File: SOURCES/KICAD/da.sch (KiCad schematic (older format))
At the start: 152 parts, among them IC301 IC_OPA1652AIDR, IC302 IC_OPA1652AIDR, IC303 IC_OPA1652AIDR, IC304 IC_OPA1652AIDR, IC305 IC_AK4458VN, IC306 IC_OPA1652AIDR, IC307 IC_OPA1652AIDR, IC308 IC_OPA1652AIDR, IC309 IC_OPA1652AIDR, X301 CONN_02X13

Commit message: Updated BOM
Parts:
- C301, C302, C309, C310, C314, C315, C321, C324, C325, C329, C330, C331, C340, C341, C345, C346, C347, C353, C356, C357: Manufacturer (none) -> Nichicon; digikey 399-6102-ND -> UVY1E101MDD-ND; pn (none) -> UVY1E101MDD
- C303, C304, C311, C312, C316, C317, C326, C327, C332, C333, C342, C343, C348, C349, C358, C359: Manufacturer (none) -> Panasonic Electronic Components; pn (none) -> ECH-U1H471GX5
- C305, C306, C318, C319, C334, C335, C350, C351: Manufacturer (none) -> KEMET; pn (none) -> C0805C270J5GACTU
- C307, C308, C322, C323, C338, C339, C354, C355: Manufacturer (none) -> Panasonic Electronic Components; pn (none) -> ECH-U1C392JX5
- C313: Manufacturer (none) -> Yageo; pn (none) -> CC0805KKX7R7BB105
- C320, C328, C336, C344, C352, C361, C362, C363, C364, C365, C366, C367, C368, C369: Manufacturer (none) -> KEMET; pn (none) -> C0805C104K5RACTU
- C337, C360: Manufacturer (none) -> Murata Electronics North America; pn (none) -> GRM21BR61E106MA73L
- IC301, IC302, IC303, IC304, IC306, IC307, IC308, IC309: Manufacturer (none) -> Texas Instruments; pn (none) -> OPA1652AIDR
- IC305: Manufacturer (none) -> AKM Semiconductor Inc.; pn (none) -> AK4458VN
- R301, R303, R311, R313, R317, R319, R328, R330, R335, R337, R345, R347, R352, R354, R368, R370: Manufacturer (none) -> Susumu; pn (none) -> RR1220P-4421-D-M
- R302, R304, R315, R316, R318, R320, R332, R333, R336, R338, R350, R351, R353, R355, R372, R373: Manufacturer (none) -> Susumu; pn (none) -> RR1220P-3401-D-M
- R305, R306, R312, R314, R321, R322, R329, R331, R339, R340, R346, R348, R357, R358, R369, R371: Manufacturer (none) -> Stackpole Electronics Inc.; pn (none) -> RNCP0805FTD150R
- R307, R308, R309, R310, R324, R325, R326, R327, R341, R342, R343, R344, R364, R365, R366, R367: Manufacturer (none) -> Yageo; pn (none) -> RT0805FRE074K7L
- R323, R334, R349, R356: Manufacturer (none) -> Yageo; pn (none) -> RC0805FR-0720RL
- R359, R360, R361, R362, R363: Manufacturer (none) -> Yageo; pn (none) -> RC0805JR-070RL
- X301: Manufacturer (none) -> Sullins Connector Solutions; pn (none) -> PRPC013DAAN-RC

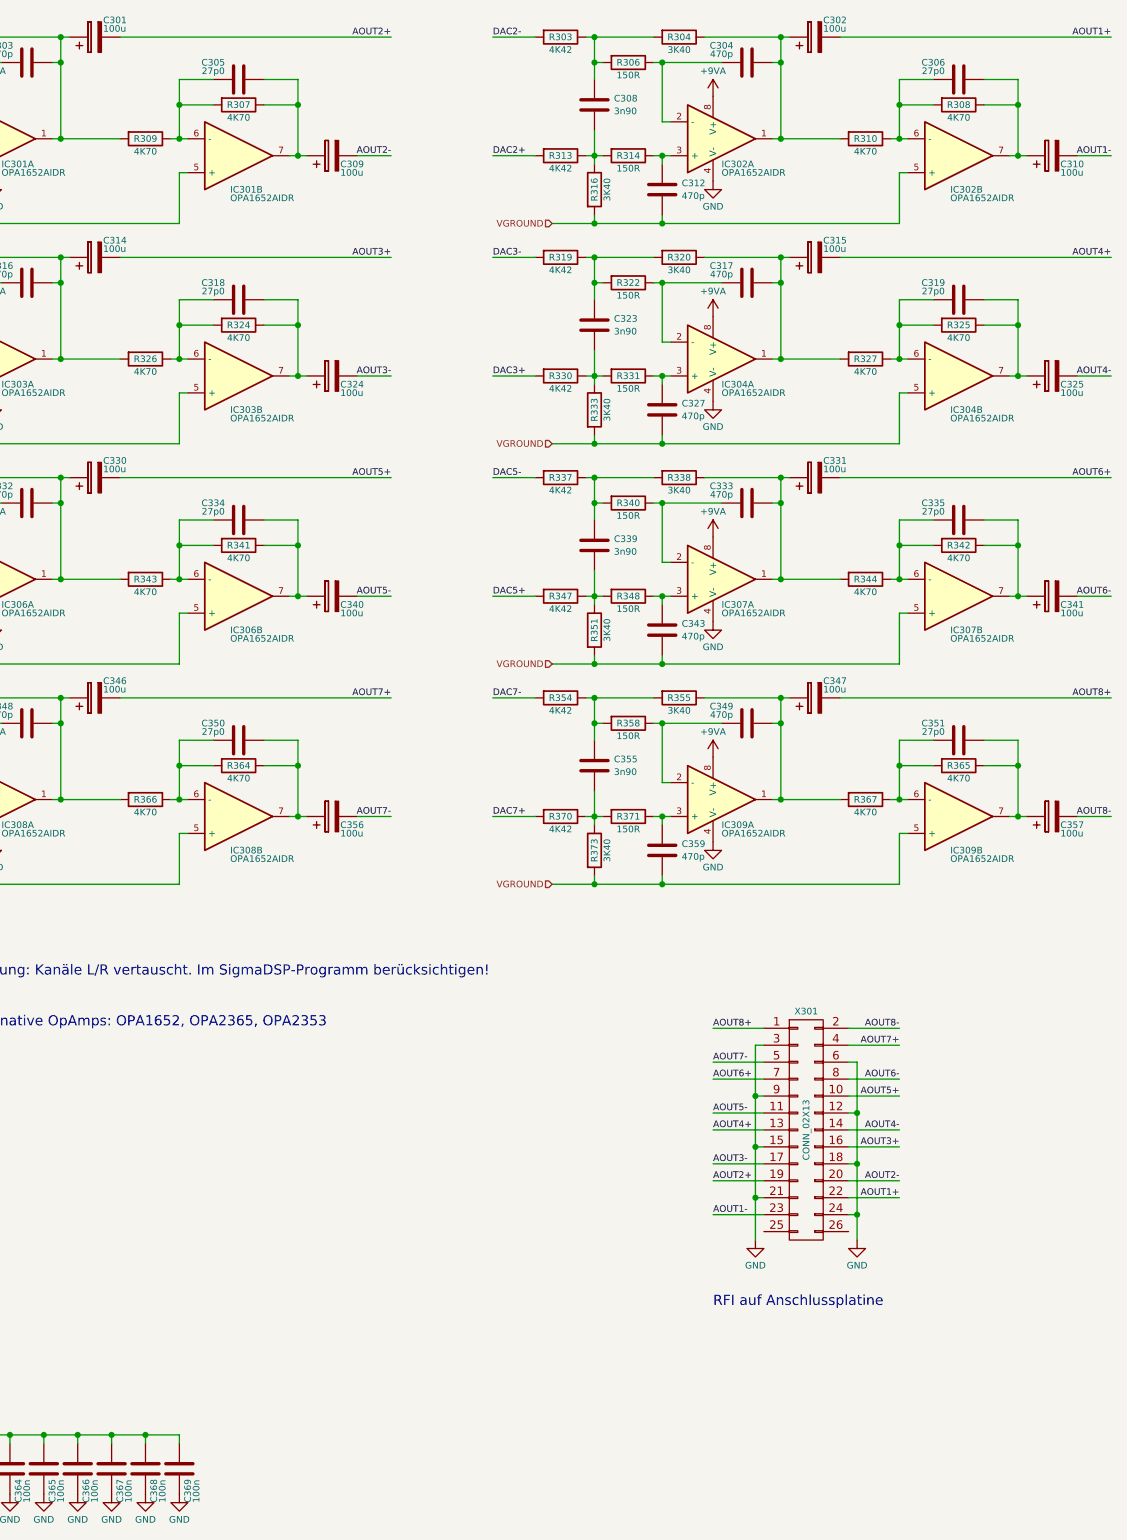
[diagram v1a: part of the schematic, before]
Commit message: Optimized DAC Output filter
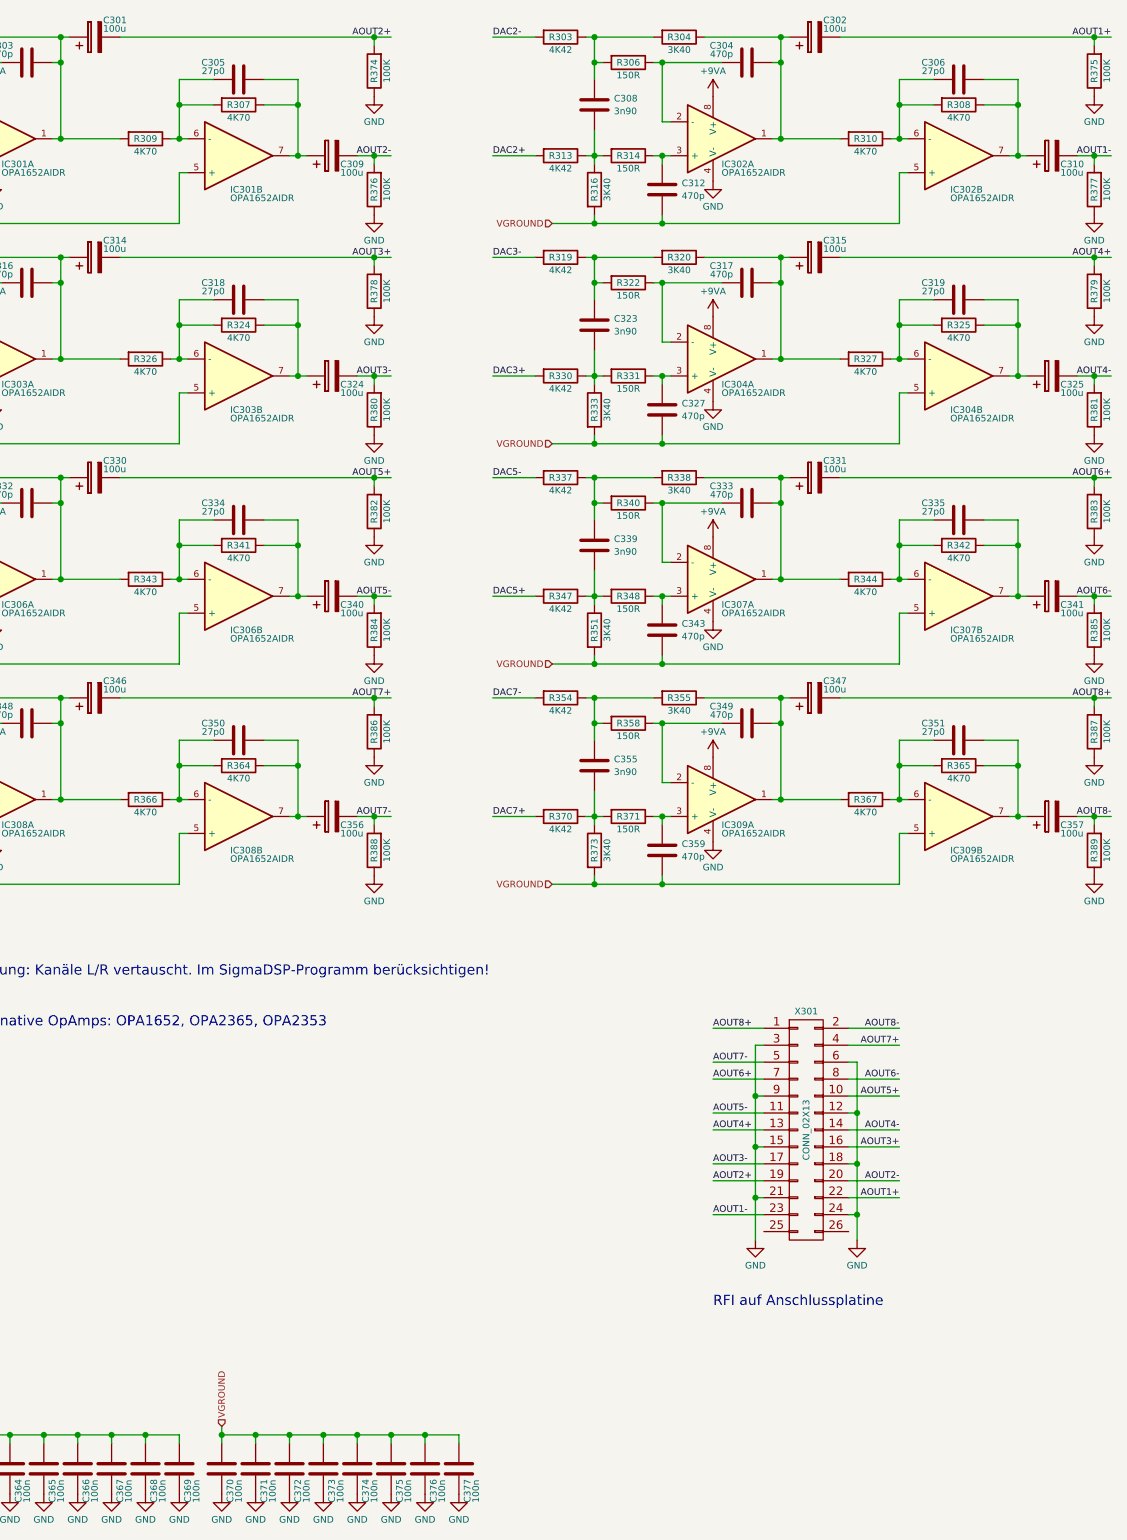
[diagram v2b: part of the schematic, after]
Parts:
- added C370, C371, C372, C373, C374, C375, C376, C377: CAP_100n_50V_X7R_0805, rklib:C0805-X7R, symbol rk:CAP_100n_50V_X7R_0805
- added R374, R375, R376, R377, R378, R379, R380, R381, R382, R383, R384, R385, R386, R387, R388, R389: RES_100K_1%_0.125W_Thick_0805, rklib:C0805-RES, symbol rk:RES_100K_1%_0.125W_Thick_0805
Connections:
- net AOUT1+: now also R375.2
- net AOUT1-: now also R377.2
- net AOUT2+: now also R374.2
- net AOUT2-: now also R376.2
- net AOUT3+: now also R378.2
- net AOUT3-: now also R380.2
- net AOUT4+: now also R379.2
- net AOUT4-: now also R381.2
- net AOUT5+: now also R382.2
- net AOUT5-: now also R384.2
- net AOUT6+: now also R383.2
- net AOUT6-: now also R385.2
- net AOUT7+: now also R386.2
- net AOUT7-: now also R388.2
- net AOUT8+: now also R387.2
- net AOUT8-: now also R389.2
- net GND: now also C370.2, C371.2, C372.2, C373.2, C374.2, C375.2, C376.2, C377.2, R374.1, R375.1, R376.1, R377.1, R378.1, R379.1, R380.1, R381.1, R382.1, R383.1, R384.1, R385.1, R386.1, R387.1, R388.1, R389.1
- net VGROUND: now also C370.1, C371.1, C372.1, C373.1, C374.1, C375.1, C376.1, C377.1
